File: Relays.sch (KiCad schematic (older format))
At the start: 12 parts, among them Q13 2N3904, Q14 2N3904, Q15 2N3904

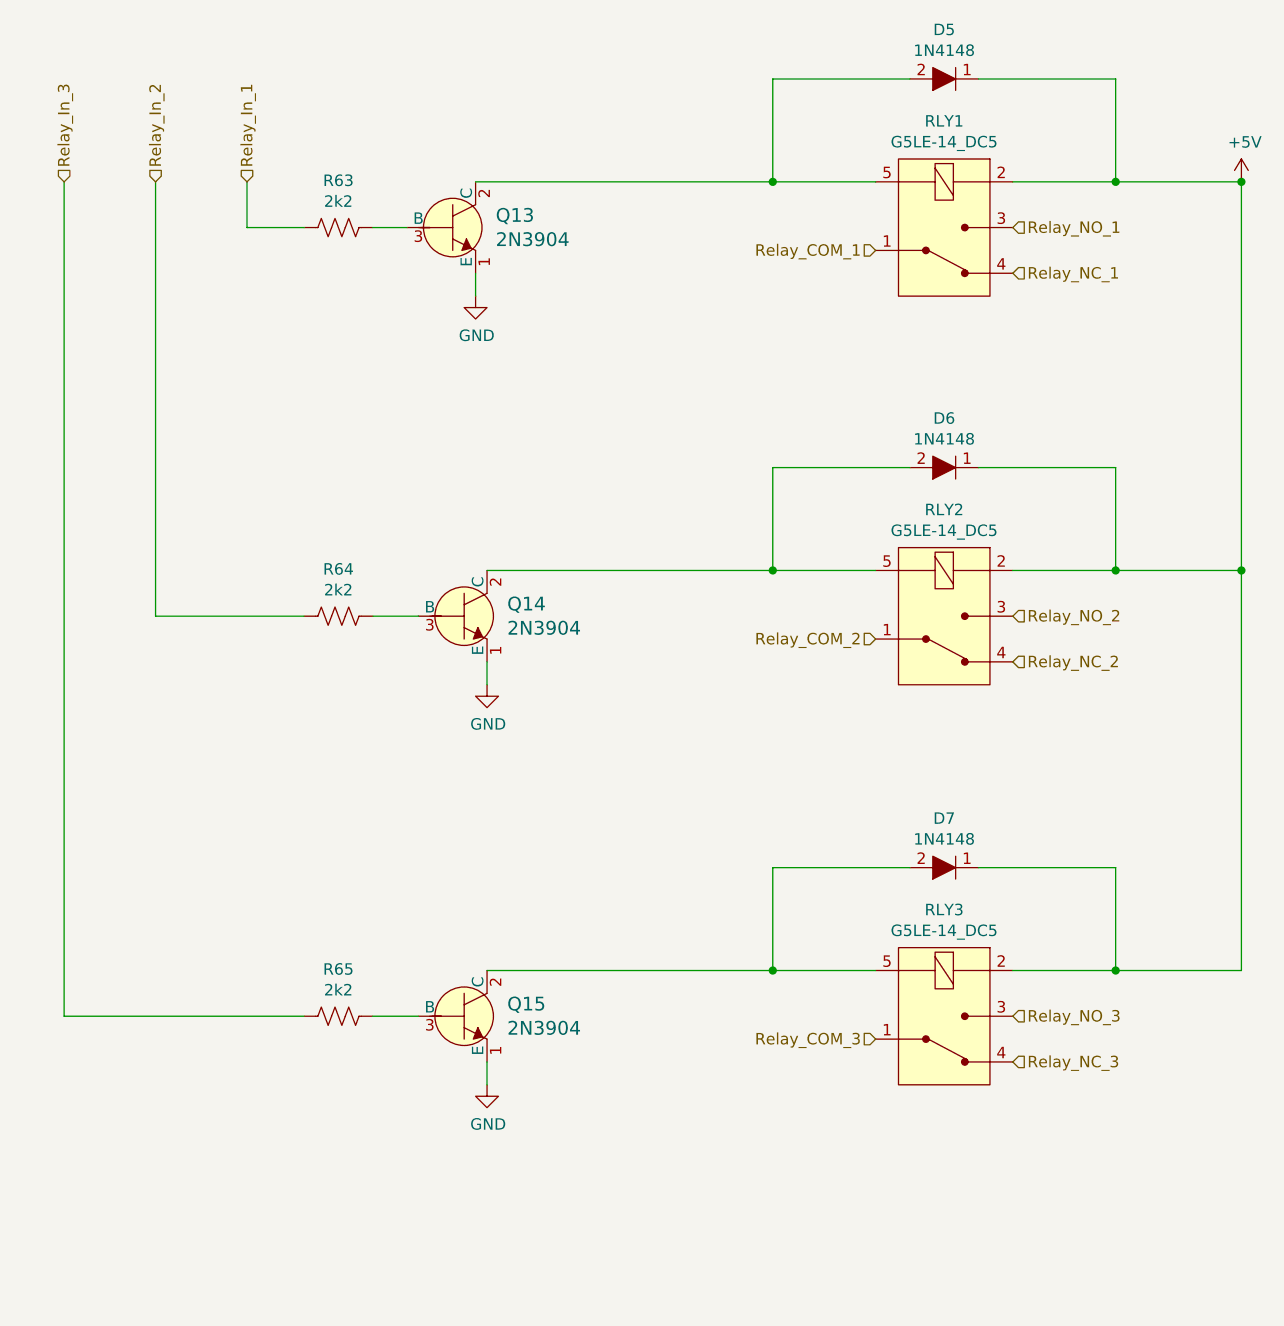
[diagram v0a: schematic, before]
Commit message: Makes it SMD based, with smaller connectors
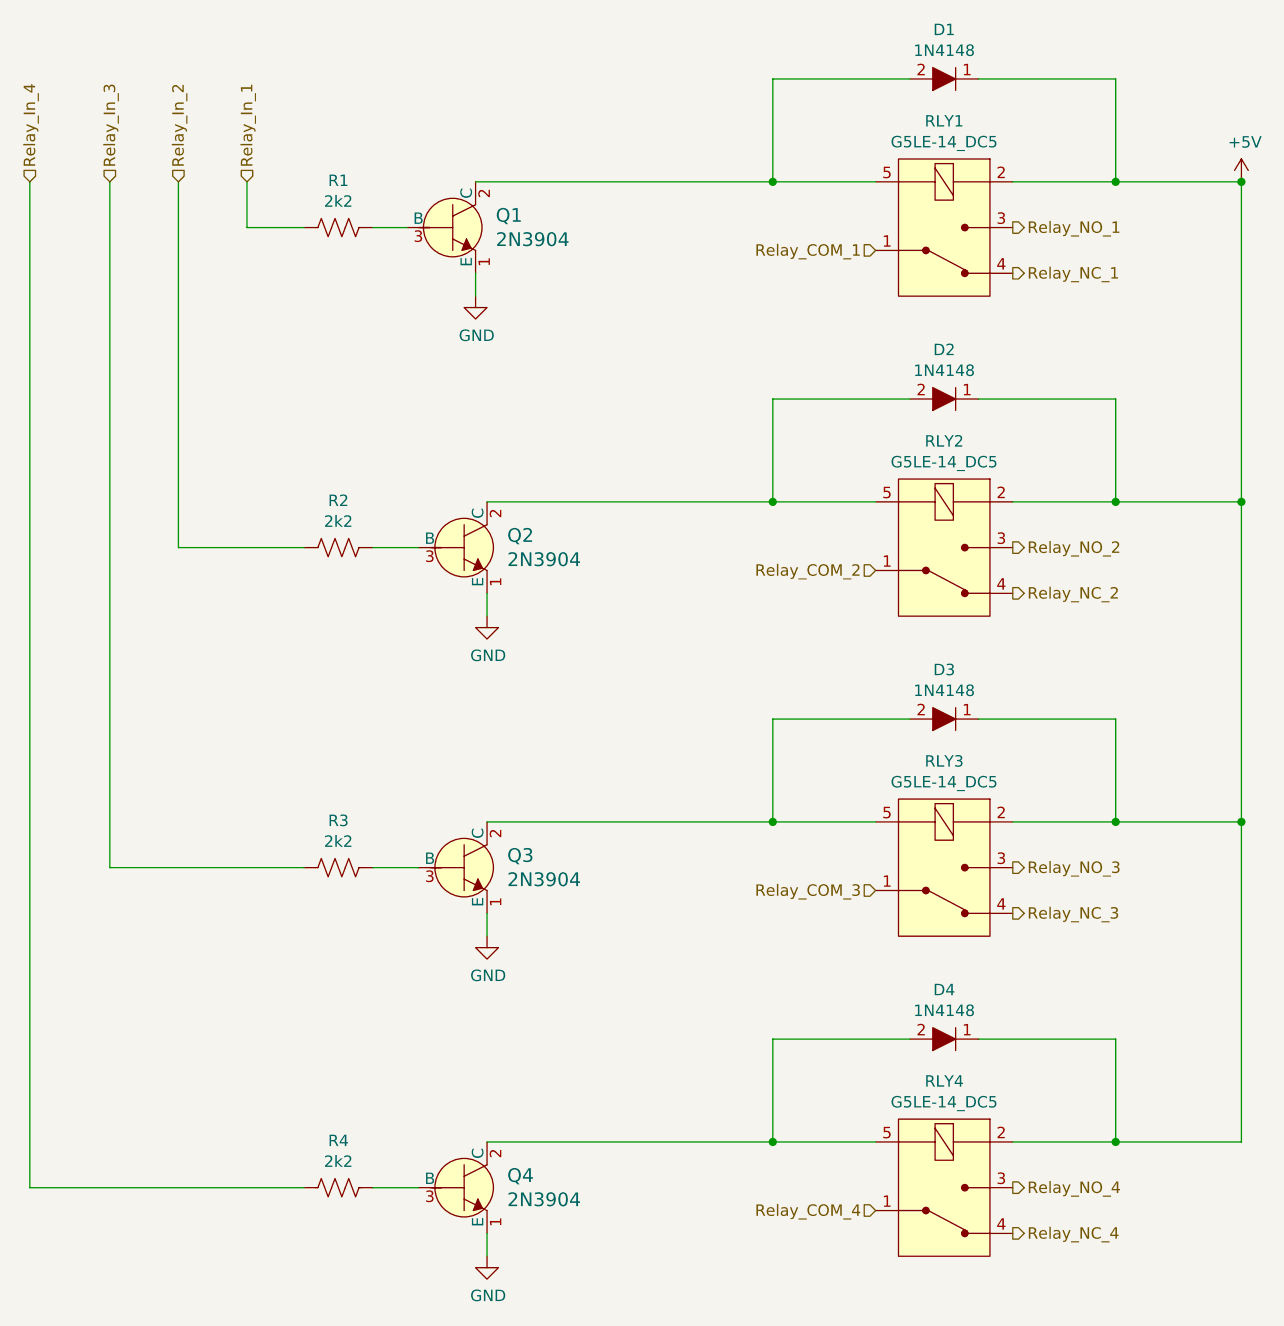
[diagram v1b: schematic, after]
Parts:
- added D4: 1N4148, Diode_SMD:D_SOD-123, symbol dk_Diodes-Rectifiers-Single:1N4148
- added Q4: 2N3904, Package_TO_SOT_SMD:SOT-23_Handsoldering, symbol dk_Transistors-Bipolar-BJT-Single:2N3904
- added R4: 2k2, Resistor_SMD:R_1206_3216Metric_Pad1.42x1.75mm_HandSolder, symbol Device:R_US
- added RLY4: G5LE-14_DC5, digikey-footprints:Relay_THT_G5LE-14, symbol dk_Power-Relays-Over-2-Amps:G5LE-14_DC5
- D1: renamed from D5; footprint digikey-footprints:Diode_DO-35_P10mm -> Diode_SMD:D_SOD-123; Digi-Key_PN 1N4148FS-ND -> MMSD4148T1GOSCT-ND; MPN 1N4148 -> MMSD4148T1G
- D2: renamed from D6; footprint digikey-footprints:Diode_DO-35_P10mm -> Diode_SMD:D_SOD-123; Digi-Key_PN 1N4148FS-ND -> MMSD4148T1GOSCT-ND; MPN 1N4148 -> MMSD4148T1G
- D3: renamed from D7; footprint digikey-footprints:Diode_DO-35_P10mm -> Diode_SMD:D_SOD-123; Digi-Key_PN 1N4148FS-ND -> MMSD4148T1GOSCT-ND; MPN 1N4148 -> MMSD4148T1G
- Q1: renamed from Q13; footprint digikey-footprints:TO-92-3 -> Package_TO_SOT_SMD:SOT-23_Handsoldering; Digi-Key_PN 2N3904CS-ND -> 1727-4044-1-ND; MPN 2N3904 -> MMBT3904,215
- Q2: renamed from Q14; footprint digikey-footprints:TO-92-3 -> Package_TO_SOT_SMD:SOT-23_Handsoldering; Digi-Key_PN 2N3904CS-ND -> 1727-4044-1-ND; MPN 2N3904 -> MMBT3904,215
- Q3: renamed from Q15; footprint digikey-footprints:TO-92-3 -> Package_TO_SOT_SMD:SOT-23_Handsoldering; Digi-Key_PN 2N3904CS-ND -> 1727-4044-1-ND; MPN 2N3904 -> MMBT3904,215
- R1: renamed from R63; footprint Resistor_THT:R_Axial_DIN0204_L3.6mm_D1.6mm_P7.62mm_Horizontal -> Resistor_SMD:R_1206_3216Metric_Pad1.42x1.75mm_HandSolder; Digi-Key_PN S2.2KCATR-ND -> A129814CT-ND; MPN (none) -> CRGCQ1206F2K2
- R2: renamed from R64; footprint Resistor_THT:R_Axial_DIN0204_L3.6mm_D1.6mm_P7.62mm_Horizontal -> Resistor_SMD:R_1206_3216Metric_Pad1.42x1.75mm_HandSolder; Digi-Key_PN S2.2KCATR-ND -> A129814CT-ND; MPN (none) -> CRGCQ1206F2K2
- R3: renamed from R65; footprint Resistor_THT:R_Axial_DIN0204_L3.6mm_D1.6mm_P7.62mm_Horizontal -> Resistor_SMD:R_1206_3216Metric_Pad1.42x1.75mm_HandSolder; Digi-Key_PN S2.2KCATR-ND -> A129814CT-ND; MPN (none) -> CRGCQ1206F2K2
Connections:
- net +5V: now also D4.1, RLY4.2 (COIL)
- net GND: now also Q4.1 (E)
- new net: D4.2, Q4.2 (C), RLY4.5 (COIL)
- new net: Q4.3 (B), R4.1
- new net Relay_COM_4: RLY4.1 (COM)
- new net Relay_In_4: R4.2
- new net Relay_NC_4: RLY4.4 (NC)
- new net Relay_NO_4: RLY4.3 (NO)
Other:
- moved on the sheet: D2, D3, Q2, Q3, R2, R3, RLY2, RLY3
